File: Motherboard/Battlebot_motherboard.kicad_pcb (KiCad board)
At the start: 2 copper layers, 42 x 61.5 mm, 30 parts, among them U1 XIAO-RP2040-SMD, U2 L9958SBTR, U3 L9958SBTR

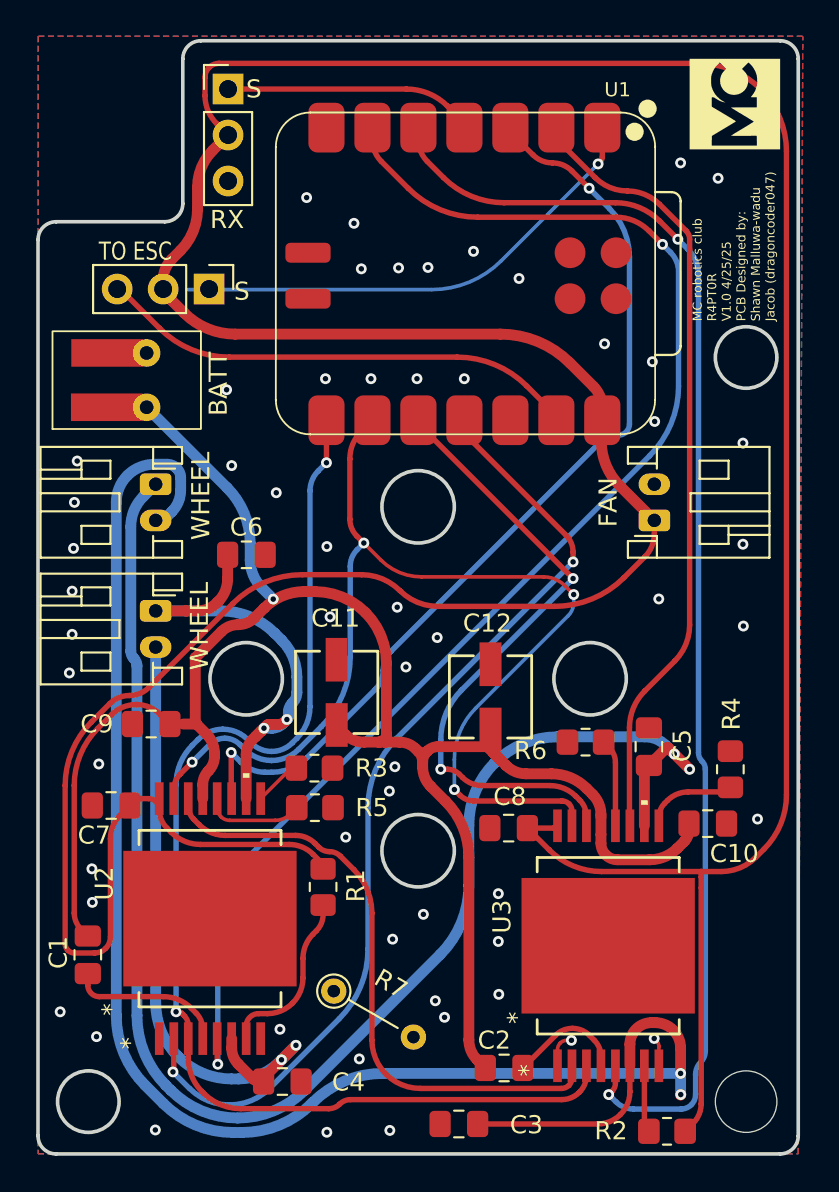
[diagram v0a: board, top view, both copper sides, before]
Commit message: removed jumper, fixed ground pours as, added 3D models for rp2040 and caps
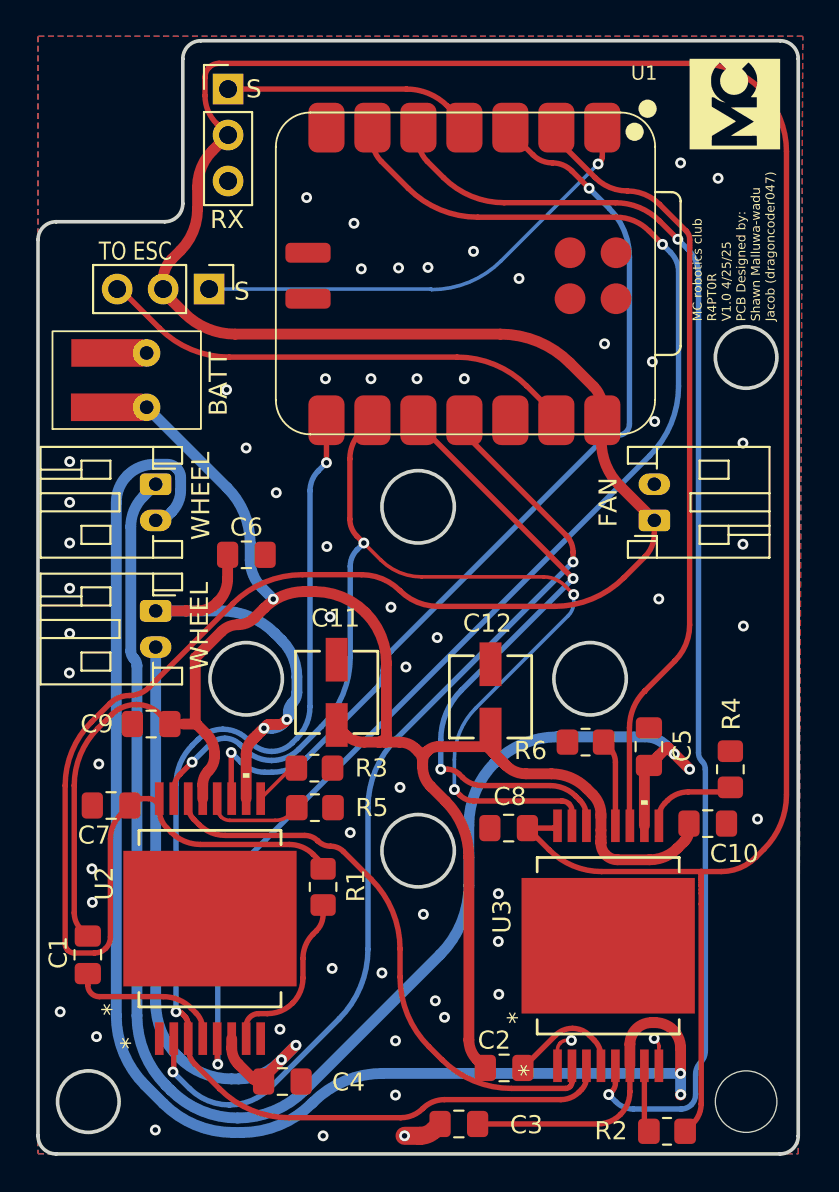
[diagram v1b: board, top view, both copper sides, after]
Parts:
- removed R7: 0, Resistor_THT:R_Axial_DIN0204_L3.6mm_D1.6mm_P5.08mm_Vertical
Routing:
- net 1SO: track 34.2 -> 31.9 mm
- net GND: track 3.54 -> 5.72 mm, vias 57 -> 58
- net PWM3: track 27.4 -> 26.2 mm
- net +12V: track 106.6 -> 107.3 mm

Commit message: updated traces one intersection
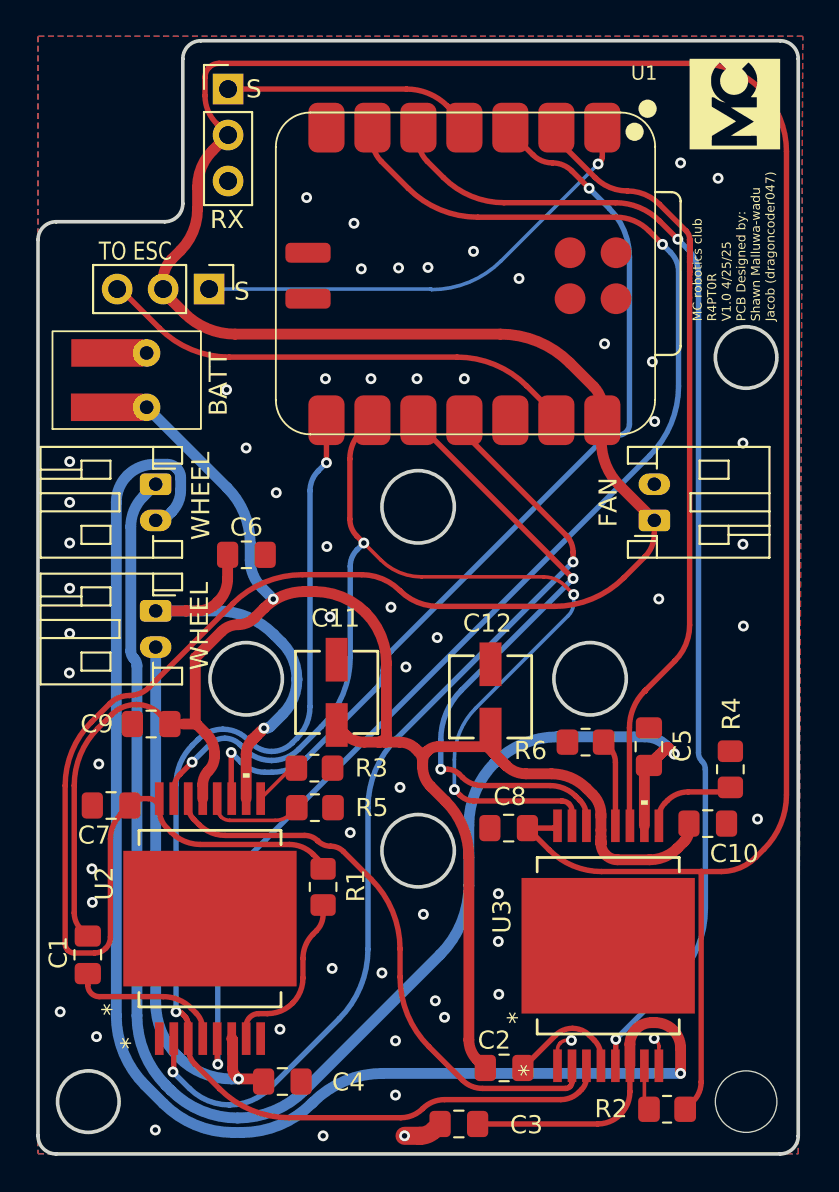
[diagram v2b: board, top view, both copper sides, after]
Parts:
- moved R2 1.22 mm to (182.8, 100.5)
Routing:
- net DIR1: track 72.3 -> 65.2 mm
- net Net-(J6-Pin_2): track 36.3 -> 30.4 mm, vias 2 -> 1
- net Net-(J6-Pin_1): track 26.5 -> 24.4 mm, vias 2 -> 1
- net +5V: track 225.4 -> 224.2 mm
- net Net-(U3-DI): track 3.70 -> 2.49 mm
- net Net-(J5-Pin_2): track 90.9 -> 89.7 mm, vias 2 -> 1
- net Net-(J5-Pin_1): track 81.8 -> 80.6 mm, vias 2 -> 1

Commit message: moved big caps farther from screws
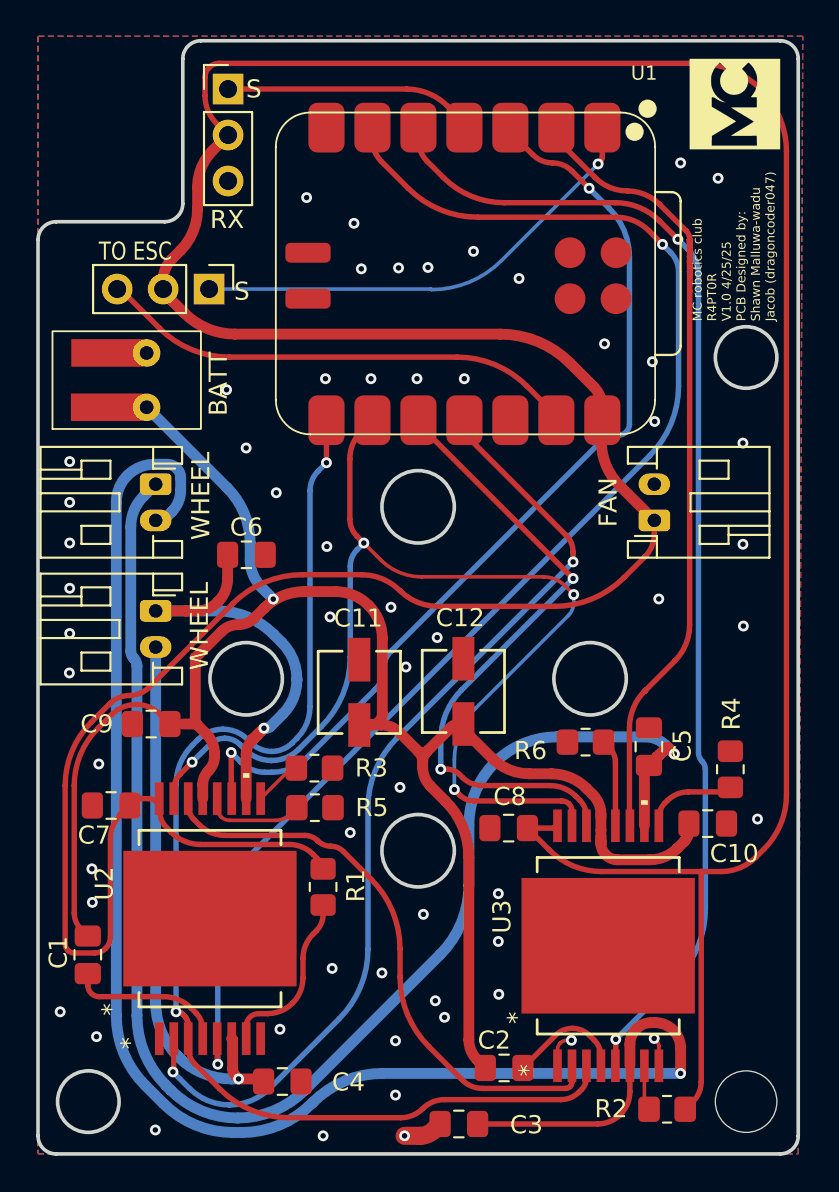
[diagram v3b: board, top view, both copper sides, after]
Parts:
- moved C12 1.53 mm to (171.5, 77.4)
- moved C11 1.25 mm to (165.8, 77.5)
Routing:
- net +12V: track 107.4 -> 103.7 mm

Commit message: copper pads
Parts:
- moved R6 0.50 mm to (178.2, 80.8)
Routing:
- net DIR1: track 65.2 -> 67.0 mm
- net Net-(J6-Pin_2): track 30.4 -> 32.0 mm
- net Net-(J5-Pin_1): track 80.6 -> 82.3 mm
- net Net-(J5-Pin_2): track 89.7 -> 91.0 mm
- net +12V: track 103.7 -> 104.5 mm
- net (no net): vias 0 -> 55
- added copper zone on B.Cu, net (none)
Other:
- board text added: "MC robotics club R4PT0R V1.0 5/2/25 PCB Designed by: Shawn Malluwa-wadu Jacob (dragoncoder047)"
- board text removed: "MC robotics club R4PT0R V1.0 4/25/25 PCB Designed by: Shawn Malluwa-wadu Jacob (dragoncoder047)"

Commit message: fix traces and stuff
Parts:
- moved R3 0.27 mm to (163.0, 81.7)
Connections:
- U2 pad EPAD: (no net) -> GND
- U3 pad EPAD: (no net) -> GND
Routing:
- net +5V: track 224.2 -> 204.1 mm, vias 0 -> 2
- net GND: vias 58 -> 113
- net (no net): vias 55 -> 0
- removed copper zone on B.Cu, net (none)
